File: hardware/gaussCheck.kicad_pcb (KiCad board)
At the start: 2 copper layers, 4 parts, among them U1 TLV493D, U2 VIM-878-DP, U3 ATSAML22N18A-AUT

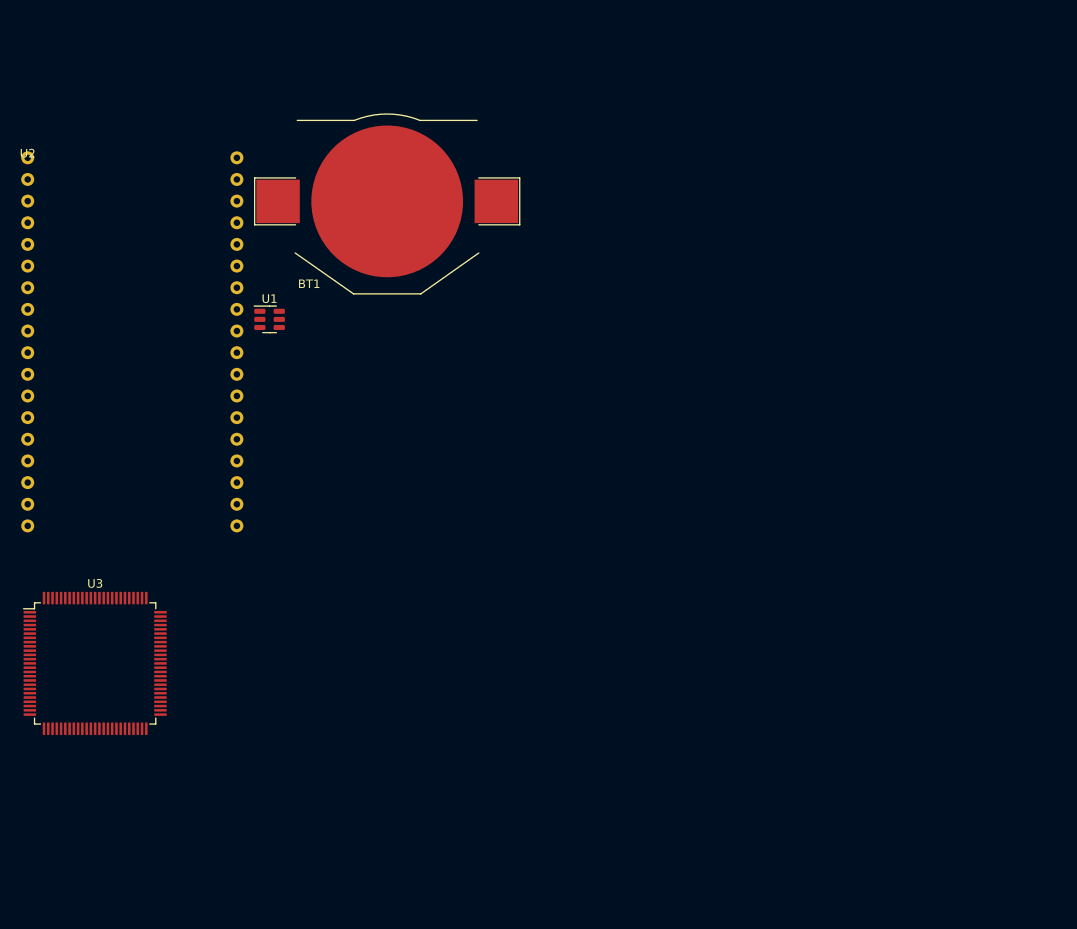
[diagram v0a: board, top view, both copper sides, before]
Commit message: SCH - display lines
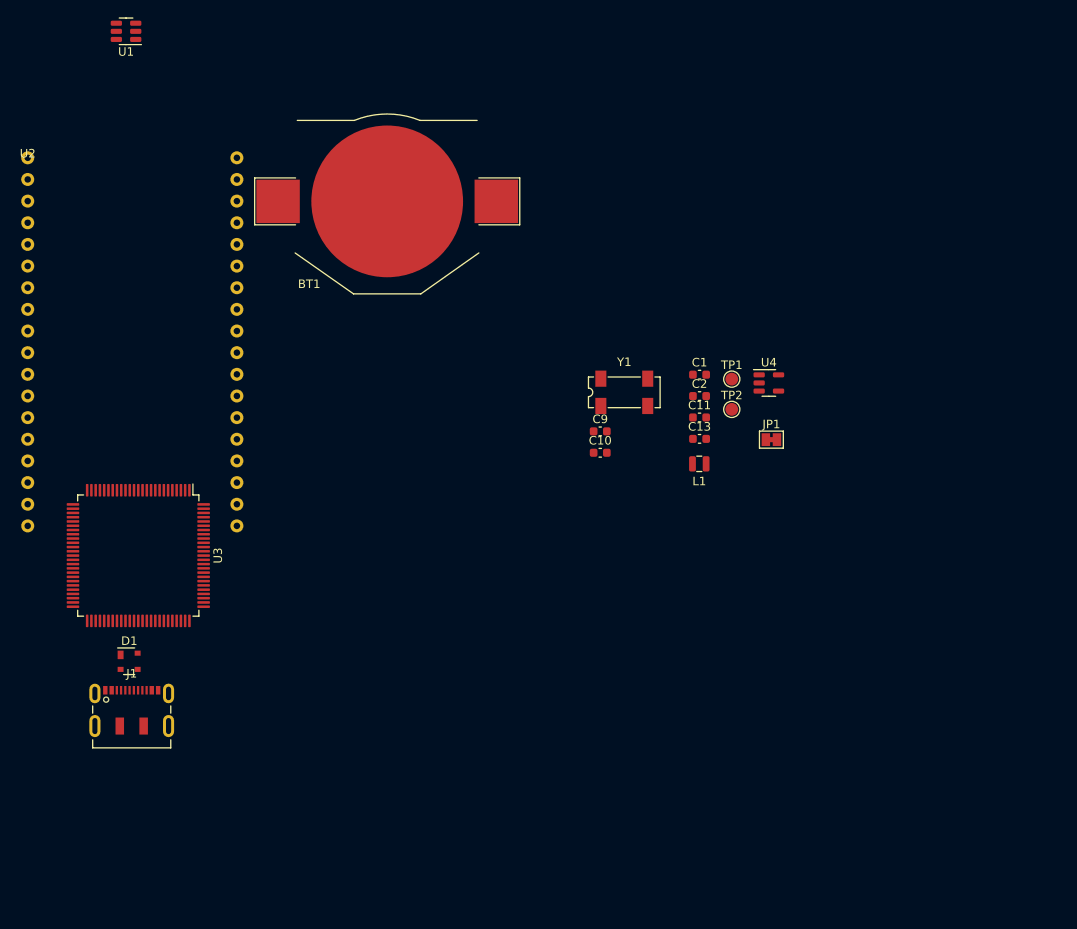
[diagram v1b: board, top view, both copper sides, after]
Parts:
- added C1: 4u7, Capacitor_SMD:C_0603_1608Metric, F.Cu at (155.5, 86.8)
- added C10: 22p, Capacitor_SMD:C_0603_1608Metric, F.Cu at (143.8, 96.0)
- added C11: 10u, Capacitor_SMD:C_0603_1608Metric, F.Cu at (155.5, 91.8)
- added C13: 4n5, Capacitor_SMD:C_0603_1608Metric, F.Cu at (155.5, 94.3)
- added C2: 10u, Capacitor_SMD:C_0603_1608Metric, F.Cu at (155.5, 89.3)
- added C9: 22p, Capacitor_SMD:C_0603_1608Metric, F.Cu at (143.8, 93.5)
- added D1: PRTR5V0U2X, Package_TO_SOT_SMD:SOT-143, F.Cu at (88.6, 120.4)
- added J1: USB_C_Receptacle_USB2.0, Connector_USB:USB_C_Receptacle_JAE_DX07S016JA1R1500, F.Cu at (88.9, 126.9)
- added JP1: IBatt, Jumper:SolderJumper-2_P1.3mm_Bridged_Pad1.0x1.5mm, F.Cu at (163.9, 94.4)
- added L1: 2u2, Knochi_Inductors:L_Murata_0806_2.00x1.60mm, F.Cu at (155.5, 97.3)
- added TP1: 3V3, TestPoint:TestPoint_Pad_D1.5mm, F.Cu at (159.3, 87.3)
- added TP2: Gnd, TestPoint:TestPoint_Pad_D1.5mm, F.Cu at (159.3, 90.9)
- added U4: TPS613221ADBV, Package_TO_SOT_SMD:SOT-23-5, F.Cu at (163.6, 87.8)
- added Y1: 32.768kHz, Crystal:Crystal_SMD_SeikoEpson_MC306-4Pin_8.0x3.2mm, F.Cu at (146.7, 88.9)
- moved U1 37.8 mm to (88.2, 46.5), turned to 180 degrees
- moved U3 13.6 mm to (89.7, 108.0), turned to -90 degrees
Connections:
- BT1 pad 1: unconnected-(BT1-+-Pad1) -> +BATT
- BT1 pad 2: unconnected-(BT1---Pad2) -> GND
- U1 pad 1: unconnected-(U1-SCL/INT-Pad1) -> /MCU/SCL
- U1 pad 2: unconnected-(U1-GND-Pad2) -> GND
- U1 pad 3: unconnected-(U1-GND-Pad3) -> GND
- U1 pad 4: unconnected-(U1-VDD-Pad4) -> +3V3
- U1 pad 5: unconnected-(U1-GND-Pad5) -> GND
- U1 pad 6: unconnected-(U1-SDA/ADDR-Pad6) -> /MCU/SDA
- U2 pad 1: unconnected-(U2-1DEFCA-Pad1) -> /MCU/DEFCA1
- U2 pad 16: unconnected-(U2-8LKJI-Pad16) -> /MCU/LKJI8
- U2 pad 17: unconnected-(U2-COM0-Pad17) -> /MCU/COM0
- U2 pad 18: unconnected-(U2-COM1-Pad18) -> /MCU/COM1
- U2 pad 19: unconnected-(U2-COM2-Pad19) -> /MCU/COM2
- U2 pad 2: unconnected-(U2-1LKJI-Pad2) -> /MCU/LKJI1
- U2 pad 20: unconnected-(U2-COM3-Pad20) -> /MCU/COM3
- U2 pad 22: unconnected-(U2-8MNGH-Pad22) -> /MCU/DPCBA8
- U2 pad 23: unconnected-(U2-7DPCBA-Pad23) -> /MCU/DPCBA7
- U2 pad 3: unconnected-(U2-2DEFCA-Pad3) -> /MCU/DEFCA2
- U2 pad 32: unconnected-(U2-8MNGH-Pad32) -> /MCU/MNGH3
- U2 pad 36: unconnected-(U2-1MNGH-Pad36) -> /MCU/MNGH1
- U3 pad 1: unconnected-(U3-PA00/XIN32/I0/SERCOM1.0-Pad1) -> Net-(U3A-PA00/XIN32/I0/SERCOM1.0)
- U3 pad 10: unconnected-(U3-PB05/I5/AIN13-Pad10) -> (no net)
- U3 pad 100: unconnected-(U3-PB03-Pad100) -> (no net)
- U3 pad 11: Net-(U3-GND-Pad11) -> GND
- U3 pad 12: VDDANA -> +3V3
- U3 pad 13: unconnected-(U3-PB06/I6/AIN14/SLCD[0]-Pad13) -> (no net)
- U3 pad 14: unconnected-(U3-PB07/SLCD[1]-Pad14) -> (no net)
- U3 pad 15: unconnected-(U3-PB08/SLCD[2]-Pad15) -> (no net)
- U3 pad 16: unconnected-(U3-PB09/SLCD[3]-Pad16) -> (no net)
- U3 pad 2: unconnected-(U3-PA01/XOUT32/I1/SERCOM1.1-Pad2) -> Net-(U3A-PA01/XOUT32/I1/SERCOM1.1)
- U3 pad 21: unconnected-(U3-PC05/SLCD[8]-Pad21) -> (no net)
- U3 pad 22: unconnected-(U3-PC06/SLCD[9}-Pad22) -> (no net)
- U3 pad 23: unconnected-(U3-PC07/SLCD[10]-Pad23) -> (no net)
- U3 pad 24: Net-(U3-GND-Pad11) -> GND
- U3 pad 25: VDDANA -> +3V3
- U3 pad 3: unconnected-(U3-PC00/I8/AIN16-Pad3) -> (no net)
- U3 pad 30: unconnected-(U3-PC08/SLCD[15]-Pad30) -> (no net)
- U3 pad 31: unconnected-(U3-PC09/SLCD[16]-Pad31) -> (no net)
- U3 pad 32: unconnected-(U3-PC10/SLCD[17]-Pad32) -> (no net)
- U3 pad 33: unconnected-(U3-PC11/SLCD[18]-Pad33) -> (no net)
- U3 pad 34: unconnected-(U3-PC12/SLCD[19]-Pad34) -> (no net)
- U3 pad 35: unconnected-(U3-PC13/SLCD[20]-Pad35) -> (no net)
- U3 pad 36: VDDIO -> +3V3
- U3 pad 37: Net-(U3-GND-Pad11) -> GND
- U3 pad 38: unconnected-(U3-VLCD-Pad38) -> Net-(U3D-VLCD)
- U3 pad 39: unconnected-(U3-PB11/SLCD[21]-Pad39) -> (no net)
- U3 pad 4: unconnected-(U3-PC01/I9/AIN17-Pad4) -> (no net)
- U3 pad 40: unconnected-(U3-PB12/SERCOM3.0|I2C/SLCD[22]-Pad40) -> (no net)
- U3 pad 41: unconnected-(U3-PB13/SERCOM3.1|I2C/SLCD[23]-Pad41) -> (no net)
- U3 pad 42: unconnected-(U3-PB14/SLCD[24]-Pad42) -> (no net)
- U3 pad 43: unconnected-(U3-PB15/SLCD[25]-Pad43) -> (no net)
- U3 pad 44: unconnected-(U3-PC14/SLCD[26]-Pad44) -> (no net)
- U3 pad 45: unconnected-(U3-PC15/SLCD[27]-Pad45) -> (no net)
- U3 pad 5: unconnected-(U3-PC02/I10/AIN18-Pad5) -> (no net)
- U3 pad 50: Net-(U3-GND-Pad11) -> GND
- U3 pad 51: VDDIO -> +3V3
- U3 pad 56: unconnected-(U3-PC16/SLCD[36]-Pad56) -> (no net)
- U3 pad 57: unconnected-(U3-PC17/SLCD[37]-Pad57) -> (no net)
- U3 pad 58: unconnected-(U3-PC18/SLCD[38]-Pad58) -> (no net)
- U3 pad 59: unconnected-(U3-PC19/SLCD[39]-Pad59) -> (no net)
- U3 pad 6: unconnected-(U3-PC03/I11/AIN19-Pad6) -> (no net)
- U3 pad 60: unconnected-(U3-PC20/SLCD[40]-Pad60) -> (no net)
- U3 pad 61: unconnected-(U3-PC21/SLCD[41]-Pad61) -> (no net)
- U3 pad 62: Net-(U3-GND-Pad11) -> GND
- U3 pad 63: VDDIO -> +3V3
- U3 pad 64: unconnected-(U3-PB16/SLCD[42]-Pad64) -> (no net)
- U3 pad 65: unconnected-(U3-PB17/SLCD[43]-Pad65) -> (no net)
- U3 pad 66: unconnected-(U3-PB18/SLCD[44]-Pad66) -> (no net)
- U3 pad 67: unconnected-(U3-PB19/SLCD[45]-Pad67) -> (no net)
- U3 pad 68: unconnected-(U3-PB20/SLCD[46]-Pad68) -> (no net)
- U3 pad 69: unconnected-(U3-PB21/SLCD[47]-Pad69) -> (no net)
- U3 pad 74: unconnected-(U3-PA24/D--Pad74) -> /MCU/D-
- U3 pad 75: unconnected-(U3-PA25/D+-Pad75) -> /MCU/D+
- U3 pad 76: Net-(U3-GND-Pad11) -> GND
- U3 pad 77: VDDIO -> +3V3
- U3 pad 78: unconnected-(U3-PB22-Pad78) -> (no net)
- U3 pad 79: unconnected-(U3-PB23-Pad79) -> (no net)
- U3 pad 80: unconnected-(U3-PB24-Pad80) -> (no net)
- U3 pad 81: unconnected-(U3-PB25-Pad81) -> (no net)
- U3 pad 82: unconnected-(U3-PC24-Pad82) -> (no net)
- U3 pad 83: unconnected-(U3-PC25-Pad83) -> (no net)
- U3 pad 84: unconnected-(U3-PC26-Pad84) -> (no net)
- U3 pad 85: unconnected-(U3-PC27-Pad85) -> (no net)
- U3 pad 86: unconnected-(U3-PC28-Pad86) -> (no net)
- U3 pad 88: unconnected-(U3-RESET-Pad88) -> /MCU/~{RESET}
- U3 pad 89: unconnected-(U3-VDDCORE-Pad89) -> Net-(U3D-VDDCORE)
- U3 pad 9: unconnected-(U3-PB04/I4/AIN12-Pad9) -> (no net)
- U3 pad 90: Net-(U3-GND-Pad11) -> GND
- U3 pad 91: unconnected-(U3-VDDOUT-Pad91) -> Net-(U3D-VDDOUT)
- U3 pad 92: VDDIO -> +3V3
- U3 pad 93: unconnected-(U3-PA30-Pad93) -> /MCU/SWDIO
- U3 pad 94: unconnected-(U3-PA31-Pad94) -> /MCU/SWCLK
- U3 pad 95: unconnected-(U3-PB30/SERCOM1.0|5.0|I2C-Pad95) -> (no net)
- U3 pad 96: unconnected-(U3-PB31/SERCOM1.1|5.1|I2C-Pad96) -> (no net)
- U3 pad 97: unconnected-(U3-PB0-Pad97) -> (no net)
- U3 pad 98: unconnected-(U3-PB1-Pad98) -> (no net)
- U3 pad 99: unconnected-(U3-PB2-Pad99) -> (no net)

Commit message: more schematic work, added buttons and led lcd wiring done
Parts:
- added C12: 100n, Capacitor_SMD:C_0603_1608Metric, F.Cu at (189.8, 56.6)
- added C14: 100n, Capacitor_SMD:C_0603_1608Metric, F.Cu at (179.7, 54.1)
- added C3: 1u, Capacitor_SMD:C_0603_1608Metric, F.Cu at (185.7, 54.1)
- added C4: 100n, Capacitor_SMD:C_0603_1608Metric, F.Cu at (185.7, 56.6)
- added C5: 100n, Capacitor_SMD:C_0603_1608Metric, F.Cu at (185.7, 59.1)
- added C6: 10u, Capacitor_SMD:C_0603_1608Metric, F.Cu at (185.7, 61.6)
- added C7: 100n, Capacitor_SMD:C_0603_1608Metric, F.Cu at (185.7, 64.1)
- added C8: 1u, Capacitor_SMD:C_0603_1608Metric, F.Cu at (189.8, 54.1)
- added D2: LED_RGB, LED_SMD:LED_RGB_Cree-PLCC-6_6x5mm_P2.1mm, F.Cu at (110.0, 111.1)
- added J2: SWD, Connector_PinHeader_1.27mm:PinHeader_2x05_P1.27mm_Vertical_SMD, F.Cu at (110.2, 95.5)
- added L2: 10uH, Inductor_SMD:L_Taiyo-Yuden_MD-4040, F.Cu at (108.1, 102.5)
- added R1: 1k, Resistor_SMD:R_0603_1608Metric, F.Cu at (189.8, 59.1)
- added R2: 10k, Resistor_SMD:R_0603_1608Metric, F.Cu at (189.8, 61.6)
- added R3: 300r, Resistor_SMD:R_0603_1608Metric, F.Cu at (189.8, 64.1)
- added R4: 1M, Resistor_SMD:R_0603_1608Metric, F.Cu at (179.7, 56.6)
- added R5: 2k2, Resistor_SMD:R_0603_1608Metric, F.Cu at (179.7, 59.1)
- added R6: 2k2, Resistor_SMD:R_0603_1608Metric, F.Cu at (179.7, 61.6)
- added R7: 330r, Resistor_SMD:R_0603_1608Metric, F.Cu at (116.5, 108.6)
- added R8: 100r, Resistor_SMD:R_0603_1608Metric, F.Cu at (116.5, 111.1)
- added R9: 100r, Resistor_SMD:R_0603_1608Metric, F.Cu at (116.5, 113.6)
- added SW1: PTS810, Button_Switch_SMD:SW_SPST_PTS810, F.Cu at (195.1, 55.2)
- added SW2: CK KSC2, Button_Switch_SMD:SW_Push_1P1T_NO_CK_KSC7xxJ, F.Cu at (172.7, 56.7)
- added SW3: CK KSC2, Button_Switch_SMD:SW_Push_1P1T_NO_CK_KSC7xxJ, F.Cu at (172.7, 64.4)
- added SW4: CK KSC2, Button_Switch_SMD:SW_Push_1P1T_NO_CK_KSC7xxJ, F.Cu at (172.7, 72.2)
- BT1: footprint Battery:BatteryHolder_Keystone_3002_1x2032 -> Battery:BatteryHolder_Keystone_3034_1x20mm; moved to B.Cu
- C10, C9: value 22p -> ??p
- Y1: footprint Crystal:Crystal_SMD_SeikoEpson_MC306-4Pin_8.0x3.2mm -> Crystal:Crystal_SMD_3215-2Pin_3.2x1.5mm
- moved BT1 52.7 mm to (89.0, 109.9), turned to 180 degrees
- moved U3 25.6 mm to (88.9, 82.5)
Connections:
- U2 pad 10: unconnected-(U2-5LKJI-Pad10) -> /MCU/LKJI5
- U2 pad 11: unconnected-(U2-6DEFCA-Pad11) -> /MCU/DEFCA6
- U2 pad 12: unconnected-(U2-6LKJI-Pad12) -> /MCU/LKJI6
- U2 pad 13: unconnected-(U2-7DEFCA-Pad13) -> /MCU/DEFCA7
- U2 pad 14: unconnected-(U2-7LKJI-Pad14) -> /MCU/LKJI7
- U2 pad 15: unconnected-(U2-8DEFCA-Pad15) -> /MCU/DEFCA8
- U2 pad 21: unconnected-(U2-8DPCBA-Pad21) -> /MCU/DPCBA8
- U2 pad 22: /MCU/DPCBA8 -> /MCU/MNGH8
- U2 pad 24: unconnected-(U2-7MNGH-Pad24) -> /MCU/MNGH7
- U2 pad 25: unconnected-(U2-6DPCBA-Pad25) -> /MCU/DPCBA6
- U2 pad 26: unconnected-(U2-6MNGH-Pad26) -> /MCU/MNGH6
- U2 pad 27: unconnected-(U2-8DPCBA-Pad27) -> /MCU/DPCBA5
- U2 pad 28: unconnected-(U2-8MNGH-Pad28) -> /MCU/MNGH5
- U2 pad 29: unconnected-(U2-8DPCBA-Pad29) -> /MCU/DPCBA4
- U2 pad 30: unconnected-(U2-8MNGH-Pad30) -> /MCU/MNGH4
- U2 pad 31: unconnected-(U2-8DPCBA-Pad31) -> /MCU/DPCBA3
- U2 pad 33: unconnected-(U2-8DPCBA-Pad33) -> /MCU/DPCBA2
- U2 pad 34: unconnected-(U2-8MNGH-Pad34) -> /MCU/MNGH2
- U2 pad 35: unconnected-(U2-1DPCBA-Pad35) -> /MCU/DPCBA1
- U2 pad 4: unconnected-(U2-2LKJI-Pad4) -> /MCU/LKJI2
- U2 pad 5: unconnected-(U2-3DEFCA-Pad5) -> /MCU/DEFCA3
- U2 pad 6: unconnected-(U2-3LKJI-Pad6) -> /MCU/LKJI3
- U2 pad 7: unconnected-(U2-4DEFCA-Pad7) -> /MCU/DEFCA4
- U2 pad 8: unconnected-(U2-4LKJI-Pad8) -> /MCU/LKJI4
- U2 pad 9: unconnected-(U2-5DEFCA-Pad9) -> /MCU/DEFCA5
- U3 pad 10: (no net) -> unconnected-(U3B-PB05/I5/AIN13-Pad10)
- U3 pad 100: (no net) -> unconnected-(U3B-PB03-Pad100)
- U3 pad 13: (no net) -> /MCU/COM0
- U3 pad 14: (no net) -> /MCU/COM1
- U3 pad 15: (no net) -> /MCU/COM2
- U3 pad 16: (no net) -> /MCU/COM3
- U3 pad 17: unconnected-(U3A-PA04/SLCD[4]-Pad17) -> /MCU/DEFCA1
- U3 pad 18: unconnected-(U3A-PA05/SLCD[5]-Pad18) -> /MCU/LKJI1
- U3 pad 19: unconnected-(U3A-PA06/SLCD[6]-Pad19) -> /MCU/MNGH1
- U3 pad 20: unconnected-(U3A-PA07/SLCD[7]-Pad20) -> /MCU/DPCBA1
- U3 pad 21: (no net) -> /MCU/DEFCA2
- U3 pad 22: (no net) -> /MCU/LKJI2
- U3 pad 23: (no net) -> /MCU/MNGH2
- U3 pad 26: unconnected-(U3A-PA08/SLCD[11]-Pad26) -> /MCU/DPCBA2
- U3 pad 27: unconnected-(U3A-PA09/SLCD[12]-Pad27) -> /MCU/DEFCA3
- U3 pad 28: unconnected-(U3A-PA10/SLCD[13]-Pad28) -> /MCU/LKJI3
- U3 pad 29: unconnected-(U3A-PA11/SLCD[14]-Pad29) -> /MCU/MNGH3
- U3 pad 3: (no net) -> /MCU/BTN1
- U3 pad 30: (no net) -> /MCU/DPCBA3
- U3 pad 31: (no net) -> /MCU/DEFCA4
- U3 pad 32: (no net) -> /MCU/LKJI4
- U3 pad 33: (no net) -> /MCU/MNGH4
- U3 pad 34: (no net) -> /MCU/DPCBA4
- U3 pad 35: (no net) -> /MCU/DEFCA5
- U3 pad 39: (no net) -> /MCU/LKJI5
- U3 pad 4: (no net) -> /MCU/BTN2
- U3 pad 40: (no net) -> /MCU/MNGH5
- U3 pad 41: (no net) -> /MCU/DPCBA5
- U3 pad 42: (no net) -> /MCU/DEFCA6
- U3 pad 43: (no net) -> /MCU/LKJI6
- U3 pad 44: (no net) -> /MCU/MNGH6
- U3 pad 45: (no net) -> /MCU/DPCBA6
- U3 pad 46: unconnected-(U3A-PA12/SERCOM3.0|4.0|I2C/SLCD[28]-Pad46) -> /MCU/DEFCA7
- U3 pad 47: unconnected-(U3A-PA13/SERCOM3.1|4.1|I2C/SLCD[29]-Pad47) -> /MCU/LKJI7
- U3 pad 48: unconnected-(U3A-PA14/SLCD[30]-Pad48) -> /MCU/MNGH7
- U3 pad 49: unconnected-(U3A-PA15/SLCD[31]-Pad49) -> /MCU/DPCBA7
- U3 pad 5: (no net) -> /MCU/BTN3
- U3 pad 52: unconnected-(U3A-PA16/SLCD[32]-Pad52) -> /MCU/DEFCA8
- U3 pad 53: unconnected-(U3A-PA17/SLCD[33]-Pad53) -> /MCU/LKJI8
- U3 pad 54: unconnected-(U3A-PA18/SLCD[34]-Pad54) -> /MCU/MNGH8
- U3 pad 55: unconnected-(U3A-PA19/SLCD[35]-Pad55) -> /MCU/DPCBA8
- U3 pad 56: (no net) -> unconnected-(U3C-PC16/SLCD[36]-Pad56)
- U3 pad 57: (no net) -> unconnected-(U3C-PC17/SLCD[37]-Pad57)
- U3 pad 58: (no net) -> unconnected-(U3C-PC18/SLCD[38]-Pad58)
- U3 pad 59: (no net) -> unconnected-(U3C-PC19/SLCD[39]-Pad59)
- U3 pad 6: (no net) -> unconnected-(U3C-PC03/I11/AIN19-Pad6)
- U3 pad 60: (no net) -> unconnected-(U3C-PC20/SLCD[40]-Pad60)
- U3 pad 61: (no net) -> unconnected-(U3C-PC21/SLCD[41]-Pad61)
- U3 pad 64: (no net) -> unconnected-(U3B-PB16/SLCD[42]-Pad64)
- U3 pad 65: (no net) -> unconnected-(U3B-PB17/SLCD[43]-Pad65)
- U3 pad 66: (no net) -> unconnected-(U3B-PB18/SLCD[44]-Pad66)
- U3 pad 67: (no net) -> unconnected-(U3B-PB19/SLCD[45]-Pad67)
- U3 pad 68: (no net) -> unconnected-(U3B-PB20/SLCD[46]-Pad68)
- U3 pad 69: (no net) -> unconnected-(U3B-PB21/SLCD[47]-Pad69)
- U3 pad 78: (no net) -> unconnected-(U3B-PB22-Pad78)
- U3 pad 79: (no net) -> unconnected-(U3B-PB23-Pad79)
- U3 pad 80: (no net) -> unconnected-(U3B-PB24-Pad80)
- U3 pad 81: (no net) -> unconnected-(U3B-PB25-Pad81)
- U3 pad 82: (no net) -> /MCU/LED1
- U3 pad 83: (no net) -> /MCU/LED2
- U3 pad 84: (no net) -> /MCU/LED3
- U3 pad 85: (no net) -> unconnected-(U3C-PC27-Pad85)
- U3 pad 86: (no net) -> unconnected-(U3C-PC28-Pad86)
- U3 pad 9: (no net) -> unconnected-(U3B-PB04/I4/AIN12-Pad9)
- U3 pad 93: /MCU/SWDIO -> /MCU/SWCLK
- U3 pad 94: /MCU/SWCLK -> /MCU/SWDIO
- U3 pad 95: (no net) -> /MCU/SDA
- U3 pad 96: (no net) -> /MCU/SCL
- U3 pad 97: (no net) -> unconnected-(U3B-PB0-Pad97)
- U3 pad 98: (no net) -> unconnected-(U3B-PB1-Pad98)
- U3 pad 99: (no net) -> unconnected-(U3B-PB2-Pad99)
- Y1 pad 2: unconnected-(Y1-Pad2) -> Net-(U3A-PA01/XOUT32/I1/SERCOM1.1)

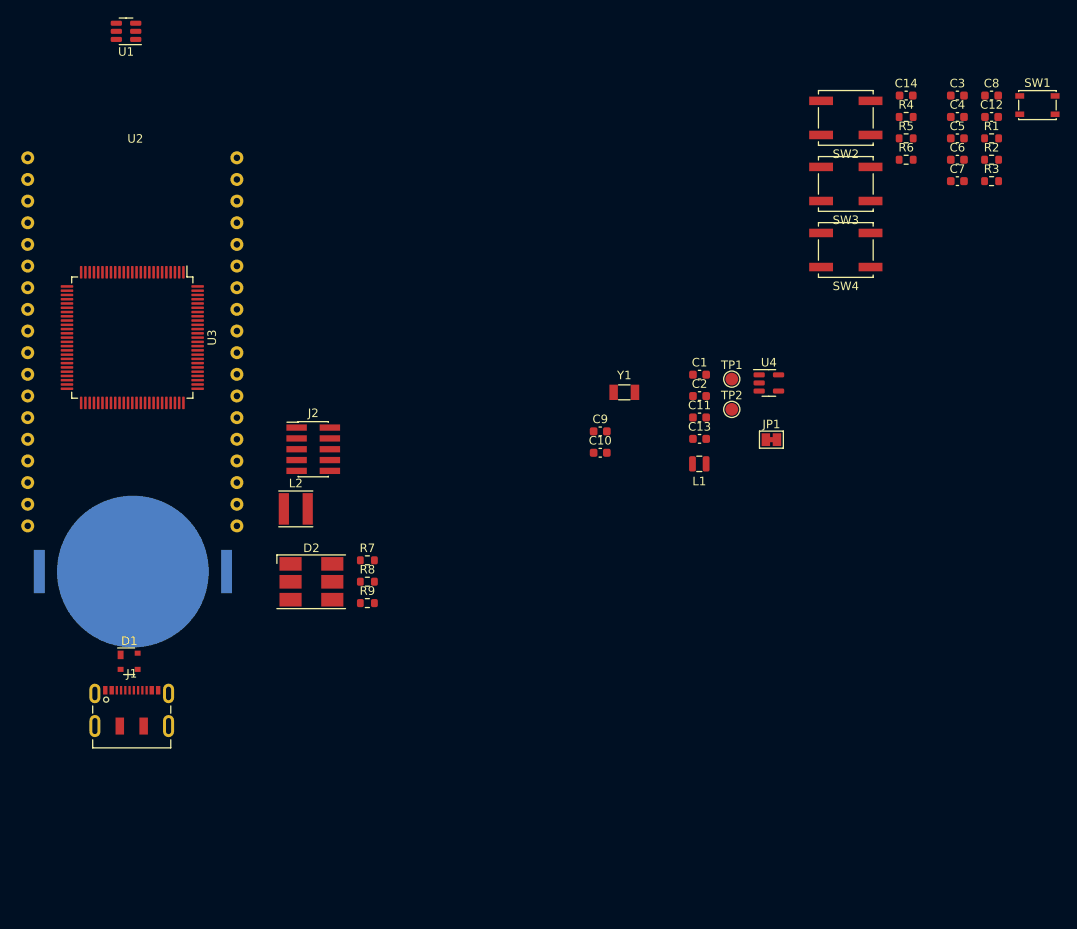
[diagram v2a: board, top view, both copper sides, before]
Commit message: try to organise on pcb
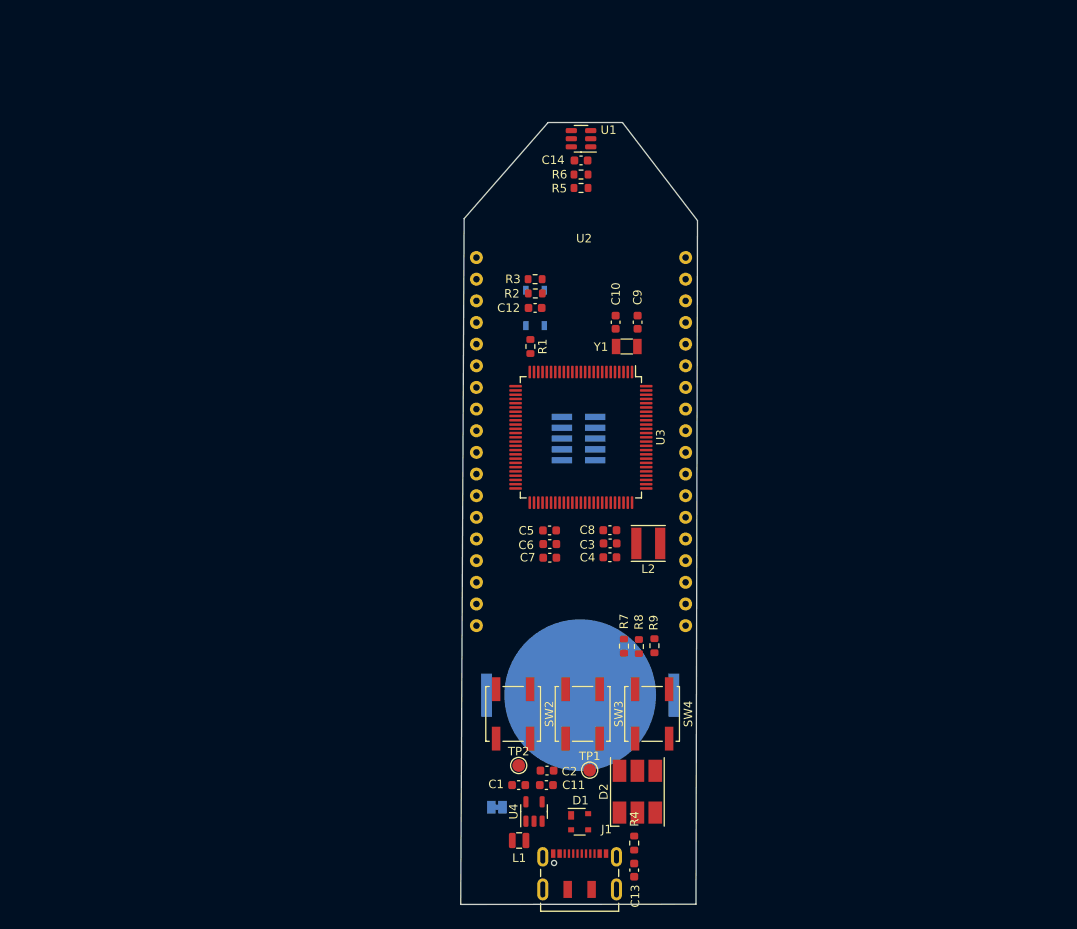
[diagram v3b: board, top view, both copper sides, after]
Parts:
- J2, JP1, SW1: moved to B.Cu
- R7: value 330r -> locked
- moved R4 91.0 mm to (147.8, 141.8), turned to 90 degrees
- moved SW2 80.1 mm to (133.6, 126.6), turned to 90 degrees
- moved SW3 69.4 mm to (141.8, 126.6), turned to 90 degrees
- moved C8 67.9 mm to (145.0, 105.0), turned to 180 degrees
- moved C3 66.5 mm to (145.0, 106.6), turned to 180 degrees
- moved C5 66.4 mm to (137.9, 105.1), turned to 180 degrees
- moved C4 65.8 mm to (145.0, 108.2), turned to 180 degrees
- moved C6 65.7 mm to (137.9, 106.7), turned to 180 degrees
- moved C7 65.1 mm to (137.9, 108.3), turned to 180 degrees
- moved SW1 63.6 mm to (136.2, 79.0), turned to 90 degrees
- moved R1 59.4 mm to (135.7, 83.5), turned to -90 degrees
- moved SW4 59.0 mm to (149.9, 126.6), turned to 90 degrees
- moved C12 58.0 mm to (136.2, 79.0), turned to 180 degrees
- moved U4 57.3 mm to (136.1, 138.1), turned to 90 degrees
- moved D1 56.1 mm to (141.4, 139.2)
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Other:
- board outline added: 27.8 x 91.7 mm

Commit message: continue
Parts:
- moved D2 71.9 mm to (141.5, 64.1), turned to 0 degrees
- moved R8 49.9 mm to (136.6, 70.2), turned to 90 degrees
- moved R9 49.9 mm to (138.2, 70.2), turned to 90 degrees
- moved R7 49.8 mm to (135.0, 70.2), turned to 90 degrees
- moved JP1 22.2 mm to (132.6, 115.3)
- moved U4 22.0 mm to (137.0, 116.1)
- moved C2 22.0 mm to (138.5, 111.3)
- moved C1 22.0 mm to (135.2, 113.0)
- moved C11 22.0 mm to (138.4, 113.0)
- moved L1 22.0 mm to (135.2, 119.5)
- moved TP1 17.6 mm to (141.1, 115.7)
- moved TP2 15.9 mm to (141.0, 118.3)
- moved C13 13.1 mm to (143.1, 132.7), turned to 180 degrees
- moved R4 8.75 mm to (143.1, 134.4), turned to 180 degrees
- moved R5 7.58 mm to (141.3, 57.3)
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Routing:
- net +3V3: track 0.00 -> 129.2 mm, vias 0 -> 5
- net /MCU/D-: track 0.00 -> 52.5 mm
- net /MCU/SDA: track 0.00 -> 49.1 mm, vias 0 -> 2
- net /MCU/D+: track 0.00 -> 48.5 mm
- net /MCU/~{RESET}: track 0.00 -> 47.8 mm, vias 0 -> 4
- net /MCU/SCL: track 0.00 -> 45.0 mm
- net /MCU/LED1: track 0.00 -> 44.9 mm
- net /MCU/DPCBA2: track 0.00 -> 44.7 mm, vias 0 -> 5
- net /MCU/LED2: track 0.00 -> 41.5 mm
- net /MCU/MNGH3: track 0.00 -> 40.2 mm, vias 0 -> 1
- net /MCU/COM1: track 0.00 -> 39.1 mm, vias 0 -> 2
- net /MCU/LED3: track 0.00 -> 37.9 mm
- net /MCU/COM0: track 0.00 -> 35.0 mm, vias 0 -> 2
- net /MCU/MNGH2: track 0.00 -> 34.1 mm, vias 0 -> 1
- net /MCU/DPCBA1: track 0.00 -> 30.7 mm, vias 0 -> 1
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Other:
- board outline removed
